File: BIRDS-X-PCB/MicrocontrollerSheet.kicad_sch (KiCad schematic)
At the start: 29 parts, among them J401 Conn_02x04_Odd_Even, J402 Conn_01x08, Q401 BSS138, Q402 BSS138, SW401 SW_Push, U401 STM32G031K8Tx, U402 MTT4B-Mini, U403 MT29F2G01ABAGDWB-IT-G_TR, Y401 ECS-2520SMV-080-FN-TR

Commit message: Fix power enable issue
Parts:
- JP403, JP404: footprint (none) -> Jumper:SolderJumper-2_P1.3mm_Open_RoundedPad1.0x1.5mm
- R404, R405, R406, R407: footprint (none) -> Resistor_SMD:R_1206_3216Metric_Pad1.30x1.75mm_HandSolder
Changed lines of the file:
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@@
       (effects (font (size 1.27 1.27)))
     )
-    (property "Footprint" "" (at 101.6 141.478 90)
+    (property "Footprint" "Resistor_SMD:R_1206_3216Metric_Pad1.30x1.75mm_HandSolder" (at 101.6 141.478 90)
       (effects (font (size 1.27 1.27)) hide)
     )
@@
       (effects (font (size 1.27 1.27)))
     )
-    (property "Footprint" "" (at 134.62 141.478 90)
+    (property "Footprint" "Resistor_SMD:R_1206_3216Metric_Pad1.30x1.75mm_HandSolder" (at 134.62 141.478 90)
       (effects (font (size 1.27 1.27)) hide)
     )
@@
       (effects (font (size 1.27 1.27)) (justify right) hide)
     )
-    (property "Footprint" "" (at 109.22 143.51 0)
+    (property "Footprint" "Jumper:SolderJumper-2_P1.3mm_Open_RoundedPad1.0x1.5mm" (at 109.22 143.51 0)
       (effects (font (size 1.27 1.27)) hide)
     )
@@
       (effects (font (size 1.27 1.27)) (justify right) hide)
     )
-    (property "Footprint" "" (at 142.24 143.51 0)
+    (property "Footprint" "Jumper:SolderJumper-2_P1.3mm_Open_RoundedPad1.0x1.5mm" (at 142.24 143.51 0)
       (effects (font (size 1.27 1.27)) hide)
     )
@@
       (effects (font (size 1.27 1.27)))
     )
-    (property "Footprint" "" (at 123.19 155.448 90)
+    (property "Footprint" "Resistor_SMD:R_1206_3216Metric_Pad1.30x1.75mm_HandSolder" (at 123.19 155.448 90)
       (effects (font (size 1.27 1.27)) hide)
     )
@@
       (effects (font (size 1.27 1.27)))
     )
-    (property "Footprint" "" (at 90.17 155.448 90)
-      (effects (font (size 1.27 1.27)) hide)
-    )
+    (property "Footprint" "Resistor_SMD:R_1206_3216Metric_Pad1.30x1.75mm_HandSolder" (at 90.17 155.448 90)
+      (effects (font (size 1.27 1.27)) hide)
+    )

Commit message: Add footprints
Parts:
- U402: footprint (none) -> BIRDS-X_Footprints_Lib:MTT4B-Mini
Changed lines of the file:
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@@
       (effects (font (size 1.27 1.27)))
     )
-    (property "Footprint" "" (at 135.89 177.8 0)
+    (property "Footprint" "BIRDS-X_Footprints_Lib:MTT4B-Mini" (at 135.89 177.8 0)
       (effects (font (size 1.27 1.27)) hide)
     )

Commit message: Finish footprints assignment
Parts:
- U403: footprint (none) -> BIRDS-X_Footprints_Lib:U-PDFN-8_6x8mm_P1.27mm
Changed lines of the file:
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@@
       (effects (font (size 1.27 1.27)))
     )
-    (property "Footprint" "" (at 208.28 140.97 0)
+    (property "Footprint" "BIRDS-X_Footprints_Lib:U-PDFN-8_6x8mm_P1.27mm" (at 208.28 140.97 0)
       (effects (font (size 1.27 1.27)) hide)
     )

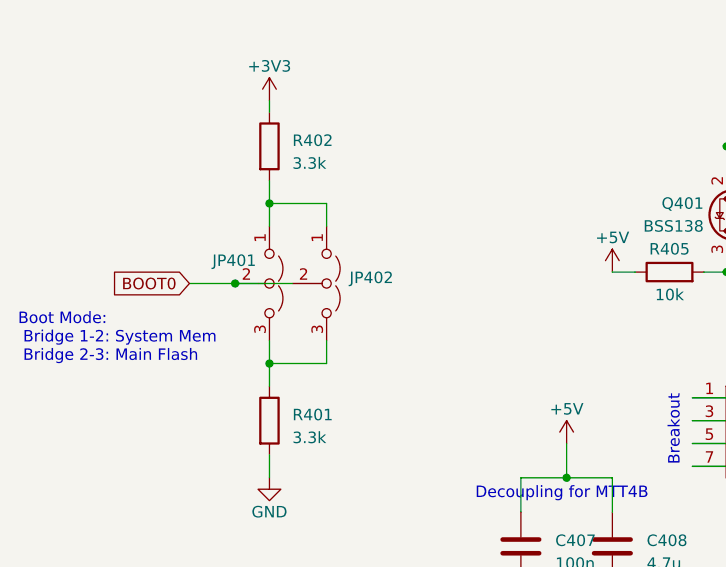
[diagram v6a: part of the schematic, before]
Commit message: Add core restricted layouts and lock them
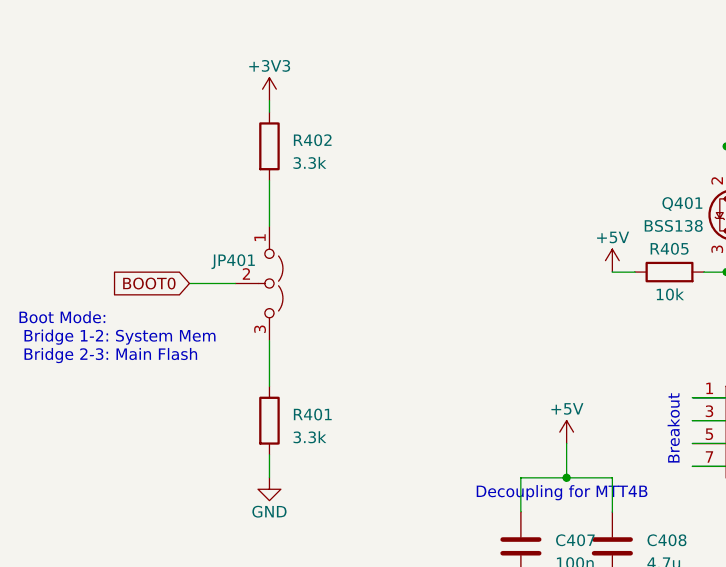
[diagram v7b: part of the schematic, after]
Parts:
- removed JP402: Jumper_3_Open, Connector_PinHeader_2.54mm:PinHeader_1x03_P2.54mm_Vertical, symbol Jumper:Jumper_3_Open
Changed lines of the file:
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@@
   (junction (at 139.7 139.7) (diameter 0) (color 0 0 0 0)
   )
-  (junction (at 41.91 154.94) (diameter 0) (color 0 0 0 0)
-  )
   (junction (at 105.41 172.72) (diameter 0) (color 0 0 0 0)
   )
@@
   (junction (at 196.85 140.97) (diameter 0) (color 0 0 0 0)
   )
-  (junction (at 45.72 146.05) (diameter 0) (color 0 0 0 0)
-  )
   (junction (at 96.52 153.67) (diameter 0) (color 0 0 0 0)
   )
@@
   )
   (junction (at 240.03 135.89) (diameter 0) (color 0 0 0 0)
-  )
-  (junction (at 45.72 163.83) (diameter 0) (color 0 0 0 0)
   )
   (junction (at 195.58 143.51) (diameter 0) (color 0 0 0 0)
@@
     (stroke (width 0) (type default))
   )
-  (wire (pts (xy 52.07 161.29) (xy 52.07 163.83))
-    (stroke (width 0) (type default))
-  )
   (wire (pts (xy 142.24 132.08) (xy 142.24 138.43))
     (stroke (width 0) (type default))
@@
     (stroke (width 0) (type default))
   )
-  (wire (pts (xy 45.72 161.29) (xy 45.72 163.83))
-    (stroke (width 0) (type default))
-  )
   (wire (pts (xy 241.3 119.38) (xy 246.38 119.38))
     (stroke (width 0) (type default))
@@
     (stroke (width 0) (type default))
   )
-  (wire (pts (xy 45.72 146.05) (xy 45.72 148.59))
-    (stroke (width 0) (type default))
-  )
   (wire (pts (xy 36.83 154.94) (xy 41.91 154.94))
     (stroke (width 0) (type default))
@@
     (stroke (width 0) (type default))
   )
-  (wire (pts (xy 45.72 163.83) (xy 45.72 166.37))
+  (wire (pts (xy 45.72 161.29) (xy 45.72 166.37))
     (stroke (width 0) (type default))
   )
@@
     (stroke (width 0) (type default))
   )
-  (wire (pts (xy 41.91 154.94) (xy 48.26 154.94))
-    (stroke (width 0) (type default))
-  )
   (wire (pts (xy 106.68 147.32) (xy 104.14 147.32))
     (stroke (width 0) (type default))
@@
     (stroke (width 0) (type default))
   )
-  (wire (pts (xy 45.72 143.51) (xy 45.72 146.05))
+  (wire (pts (xy 45.72 143.51) (xy 45.72 148.59))
     (stroke (width 0) (type default))
   )
@@
     (stroke (width 0) (type default))
   )
-  (wire (pts (xy 52.07 146.05) (xy 45.72 146.05))
-    (stroke (width 0) (type default))
-  )
   (wire (pts (xy 107.95 165.1) (xy 107.95 172.72))
     (stroke (width 0) (type default))
@@
     (stroke (width 0) (type default))
   )
-  (wire (pts (xy 52.07 148.59) (xy 52.07 146.05))
-    (stroke (width 0) (type default))
-  )
   (wire (pts (xy 83.82 191.77) (xy 83.82 187.96))
-    (stroke (width 0) (type default))
-  )
-  (wire (pts (xy 45.72 163.83) (xy 52.07 163.83))
     (stroke (width 0) (type default))
   )
@@
         )
       )
-    )
-  )
-  (symbol (lib_id "Jumper:Jumper_3_Open") (at 52.07 154.94 270) (unit 1)
-    (in_bom yes) (on_board yes) (dnp no) (fields_autoplaced)
-    (property "Reference" "JP402" (at 54.61 154.305 90)
-      (effects (font (size 1.27 1.27)) (justify left))
-    )
-    (property "Value" "Jumper_3_Open" (at 54.61 156.845 90)
-      (effects (font (size 1.27 1.27)) (justify left) hide)
-    )
-    (property "Footprint" "Connector_PinHeader_2.54mm:PinHeader_1x03_P2.54mm_Vertical" (at 52.07 154.94 0)
-      (effects (font (size 1.27 1.27)) hide)
-    )
-    (property "Datasheet" "~" (at 52.07 154.94 0)
-      (effects (font (size 1.27 1.27)) hide)
-    )
-    (pin "1")
-    (pin "2")
-    (pin "3")
-    (instances
-      (project "BIRDS-X-PCB"
-        (path "/c2796b15-795a-4d6e-ad4b-0ba87ded4bc9/d490f402-3a4d-40a5-b165-30c74c6560b7"
-          (reference "JP402") (unit 1)
-        )
-      )

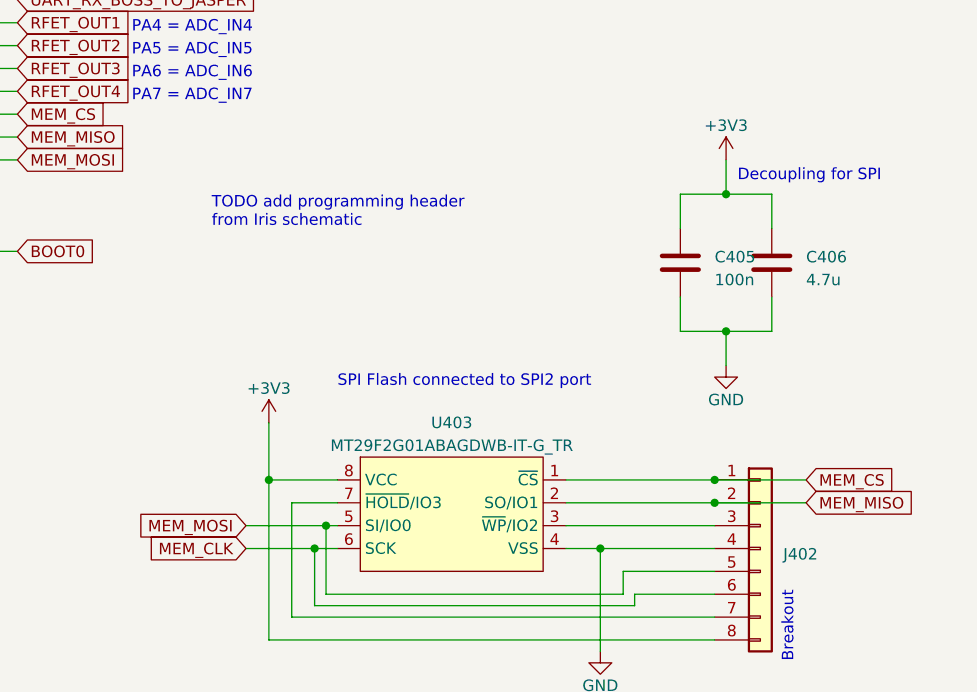
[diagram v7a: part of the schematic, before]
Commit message: Fix flash signals, fix footprints
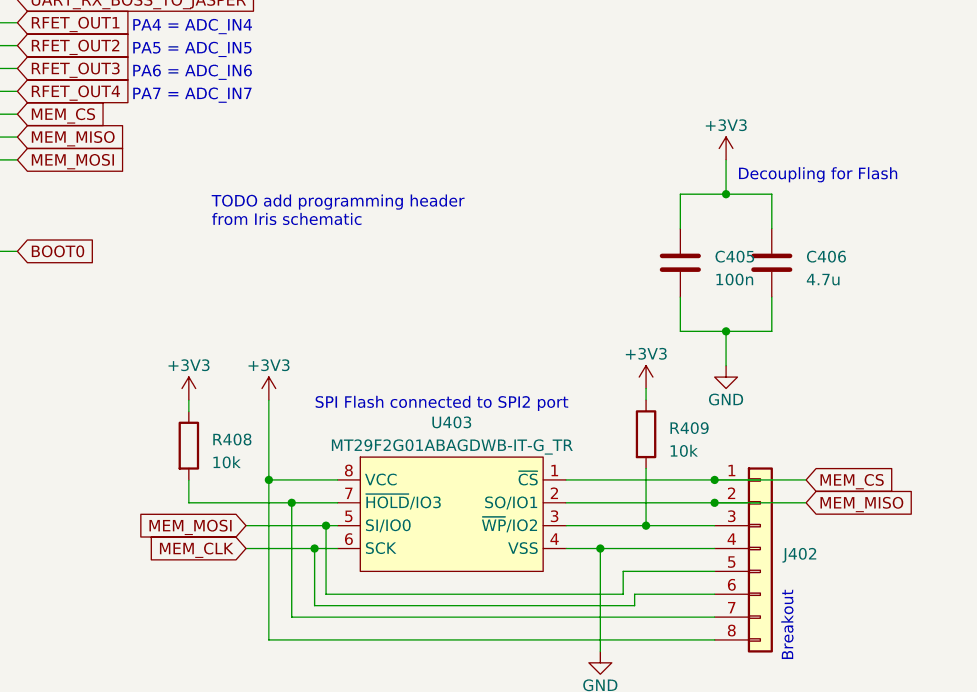
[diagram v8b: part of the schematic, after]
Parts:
- added R408, R409: 10k, Resistor_SMD:R_1206_3216Metric_Pad1.30x1.75mm_HandSolder, symbol Device:R
- SW401: footprint Button_Switch_SMD:SW_SPST_EVPBF -> Button_Switch_SMD:SW_Push_SPST_NO_Alps_SKRK
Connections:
- net +3V3: now also R408.1, R409.1
- net at J402.3 (Pin_3), U403.3 (~{WP}/IO2): now also R409.2
- net at J402.7 (Pin_7), U403.7 (~{HOLD}/IO3): now also R408.2
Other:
- note added: "Decoupling for Flash"
- note removed: "Decoupling for SPI"
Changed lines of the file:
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@@
   (junction (at 241.3 119.38) (diameter 0) (color 0 0 0 0)
   )
+  (junction (at 193.04 138.43) (diameter 0) (color 0 0 0 0)
+  )
   (junction (at 78.74 176.53) (diameter 0) (color 0 0 0 0)
   )
@@
   )
   (junction (at 113.03 170.18) (diameter 0) (color 0 0 0 0)
+  )
+  (junction (at 232.41 140.97) (diameter 0) (color 0 0 0 0)
   )
   (junction (at 109.22 58.42) (diameter 0) (color 0 0 0 0)
@@
     (stroke (width 0) (type default))
   )
+  (wire (pts (xy 193.04 138.43) (xy 181.61 138.43))
+    (stroke (width 0) (type default))
+  )
   (wire (pts (xy 73.66 187.96) (xy 73.66 191.77))
     (stroke (width 0) (type default))
@@
     (stroke (width 0) (type default))
   )
+  (wire (pts (xy 232.41 134.62) (xy 232.41 140.97))
+    (stroke (width 0) (type default))
+  )
   (wire (pts (xy 82.55 82.55) (xy 85.09 82.55))
     (stroke (width 0) (type default))
@@
     (stroke (width 0) (type default))
   )
+  (wire (pts (xy 181.61 127) (xy 181.61 128.27))
+    (stroke (width 0) (type default))
+  )
   (wire (pts (xy 113.03 170.18) (xy 119.38 170.18))
     (stroke (width 0) (type default))
@@
     (stroke (width 0) (type default))
   )
+  (wire (pts (xy 232.41 125.73) (xy 232.41 127))
+    (stroke (width 0) (type default))
+  )
   (wire (pts (xy 36.83 154.94) (xy 41.91 154.94))
     (stroke (width 0) (type default))
@@
     (stroke (width 0) (type default))
   )
-  (wire (pts (xy 223.52 140.97) (xy 240.03 140.97))
+  (wire (pts (xy 223.52 140.97) (xy 232.41 140.97))
     (stroke (width 0) (type default))
   )
@@
     (stroke (width 0) (type default))
   )
+  (wire (pts (xy 181.61 138.43) (xy 181.61 135.89))
+    (stroke (width 0) (type default))
+  )
   (wire (pts (xy 116.84 100.33) (xy 125.73 100.33))
     (stroke (width 0) (type default))
@@
     (stroke (width 0) (type default))
   )
+  (wire (pts (xy 232.41 140.97) (xy 240.03 140.97))
+    (stroke (width 0) (type default))
+  )
   (wire (pts (xy 196.85 148.59) (xy 229.87 148.59))
     (stroke (width 0) (type default))
@@
     (stroke (width 0) (type default))
   )
-  (wire (pts (xy 190.5 129.54) (xy 190.5 135.89))
+  (wire (pts (xy 190.5 127) (xy 190.5 135.89))
     (stroke (width 0) (type default))
   )
@@
     (effects (font (size 1.27 1.27)) (justify left bottom))
   )
-  (text "SPI Flash connected to SPI2 port" (at 198.12 125.73 0)
+  (text "SPI Flash connected to SPI2 port" (at 195.58 128.27 0)
     (effects (font (size 1.27 1.27)) (justify left bottom))
   )
@@
     (effects (font (size 1.27 1.27)) (justify left bottom))
   )
-  (text "Decoupling for SPI" (at 242.57 102.87 0)
+  (text "Decoupling for Flash" (at 242.57 102.87 0)
     (effects (font (size 1.27 1.27)) (justify left bottom))
   )
@@
     )
   )
+  (symbol (lib_id "Device:R") (at 181.61 132.08 0) (unit 1)
+    (in_bom yes) (on_board yes) (dnp no) (fields_autoplaced)
+    (property "Reference" "R408" (at 184.15 131.445 0)
+      (effects (font (size 1.27 1.27)) (justify left))
+    )
+    (property "Value" "10k" (at 184.15 133.985 0)
+      (effects (font (size 1.27 1.27)) (justify left))
+    )
+    (property "Footprint" "Resistor_SMD:R_1206_3216Metric_Pad1.30x1.75mm_HandSolder" (at 179.832 132.08 90)
+      (effects (font (size 1.27 1.27)) hide)
+    )
+    (property "Datasheet" "~" (at 181.61 132.08 0)
+      (effects (font (size 1.27 1.27)) hide)
+    )
+    (pin "1")
+    (pin "2")
+    (instances
+      (project "BIRDS-X-PCB"
+        (path "/c2796b15-795a-4d6e-ad4b-0ba87ded4bc9/d490f402-3a4d-40a5-b165-30c74c6560b7"
+          (reference "R408") (unit 1)
+        )
+      )
+    )
+  )
   (symbol (lib_id "power:GND") (at 227.33 154.94 0) (unit 1)
     (in_bom yes) (on_board yes) (dnp no)
@@
         (path "/c2796b15-795a-4d6e-ad4b-0ba87ded4bc9/d490f402-3a4d-40a5-b165-30c74c6560b7"
           (reference "R407") (unit 1)
+        )
+      )
+    )
+  )
+  (symbol (lib_id "Device:R") (at 232.41 130.81 0) (unit 1)
+    (in_bom yes) (on_board yes) (dnp no) (fields_autoplaced)
+    (property "Reference" "R409" (at 234.95 130.175 0)
+      (effects (font (size 1.27 1.27)) (justify left))
+    )
+    (property "Value" "10k" (at 234.95 132.715 0)
+      (effects (font (size 1.27 1.27)) (justify left))
+    )
+    (property "Footprint" "Resistor_SMD:R_1206_3216Metric_Pad1.30x1.75mm_HandSolder" (at 230.632 130.81 90)
+      (effects (font (size 1.27 1.27)) hide)
+    )
+    (property "Datasheet" "~" (at 232.41 130.81 0)
+      (effects (font (size 1.27 1.27)) hide)
+    )
+    (pin "1")
+    (pin "2")
+    (instances
+      (project "BIRDS-X-PCB"
+        (path "/c2796b15-795a-4d6e-ad4b-0ba87ded4bc9/d490f402-3a4d-40a5-b165-30c74c6560b7"
+          (reference "R409") (unit 1)
         )
       )
@@
     )
   )
-  (symbol (lib_id "power:+3V3") (at 190.5 129.54 0) (unit 1)
-    (in_bom yes) (on_board yes) (dnp no) (fields_autoplaced)
-    (property "Reference" "#PWR0410" (at 190.5 133.35 0)
-      (effects (font (size 1.27 1.27)) hide)
-    )
-    (property "Value" "+3V3" (at 190.5 125.73 0)
-      (effects (font (size 1.27 1.27)))
-    )
-    (property "Footprint" "" (at 190.5 129.54 0)
-      (effects (font (size 1.27 1.27)) hide)
-    )
-    (property "Datasheet" "" (at 190.5 129.54 0)
+  (symbol (lib_id "power:+3V3") (at 190.5 127 0) (unit 1)
+    (in_bom yes) (on_board yes) (dnp no) (fields_autoplaced)
+    (property "Reference" "#PWR0410" (at 190.5 130.81 0)
+      (effects (font (size 1.27 1.27)) hide)
+    )
+    (property "Value" "+3V3" (at 190.5 123.19 0)
+      (effects (font (size 1.27 1.27)))
+    )
+    (property "Footprint" "" (at 190.5 127 0)
+      (effects (font (size 1.27 1.27)) hide)
+    )
+    (property "Datasheet" "" (at 190.5 127 0)
       (effects (font (size 1.27 1.27)) hide)
     )
@@
       (effects (font (size 1.27 1.27)) (justify right))
     )
-    (property "Footprint" "Button_Switch_SMD:SW_SPST_EVPBF" (at 91.44 64.77 0)
+    (property "Footprint" "Button_Switch_SMD:SW_Push_SPST_NO_Alps_SKRK" (at 91.44 64.77 0)
       (effects (font (size 1.27 1.27)) hide)
     )
@@
     )
   )
+  (symbol (lib_id "power:+3V3") (at 232.41 125.73 0) (unit 1)
+    (in_bom yes) (on_board yes) (dnp no) (fields_autoplaced)
+    (property "Reference" "#PWR0425" (at 232.41 129.54 0)
+      (effects (font (size 1.27 1.27)) hide)
+    )
+    (property "Value" "+3V3" (at 232.41 121.92 0)
+      (effects (font (size 1.27 1.27)))
+    )
+    (property "Footprint" "" (at 232.41 125.73 0)
+      (effects (font (size 1.27 1.27)) hide)
+    )
+    (property "Datasheet" "" (at 232.41 125.73 0)
+      (effects (font (size 1.27 1.27)) hide)
+    )
+    (pin "1")
+    (instances
+      (project "BIRDS-X-PCB"
+        (path "/c2796b15-795a-4d6e-ad4b-0ba87ded4bc9/d490f402-3a4d-40a5-b165-30c74c6560b7"
+          (reference "#PWR0425") (unit 1)
+        )
+      )
+    )
+  )
   (symbol (lib_id "Jumper:Jumper_3_Open") (at 45.72 154.94 270) (unit 1)
     (in_bom yes) (on_board yes) (dnp no)
@@
         )
       )
+    )
+  )
+  (symbol (lib_id "power:+3V3") (at 181.61 127 0) (unit 1)
+    (in_bom yes) (on_board yes) (dnp no) (fields_autoplaced)
+    (property "Reference" "#PWR0424" (at 181.61 130.81 0)
+      (effects (font (size 1.27 1.27)) hide)
+    )
+    (property "Value" "+3V3" (at 181.61 123.19 0)
+      (effects (font (size 1.27 1.27)))
+    )
+    (property "Footprint" "" (at 181.61 127 0)
+      (effects (font (size 1.27 1.27)) hide)
+    )
+    (property "Datasheet" "" (at 181.61 127 0)
+      (effects (font (size 1.27 1.27)) hide)
+    )
+    (pin "1")
+    (instances
+      (project "BIRDS-X-PCB"
+        (path "/c2796b15-795a-4d6e-ad4b-0ba87ded4bc9/d490f402-3a4d-40a5-b165-30c74c6560b7"
+          (reference "#PWR0424") (unit 1)
+        )
+      )
